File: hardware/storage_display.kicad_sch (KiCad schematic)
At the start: 14 parts, among them J2 microSD, J3 OLED 1.27in 128x96

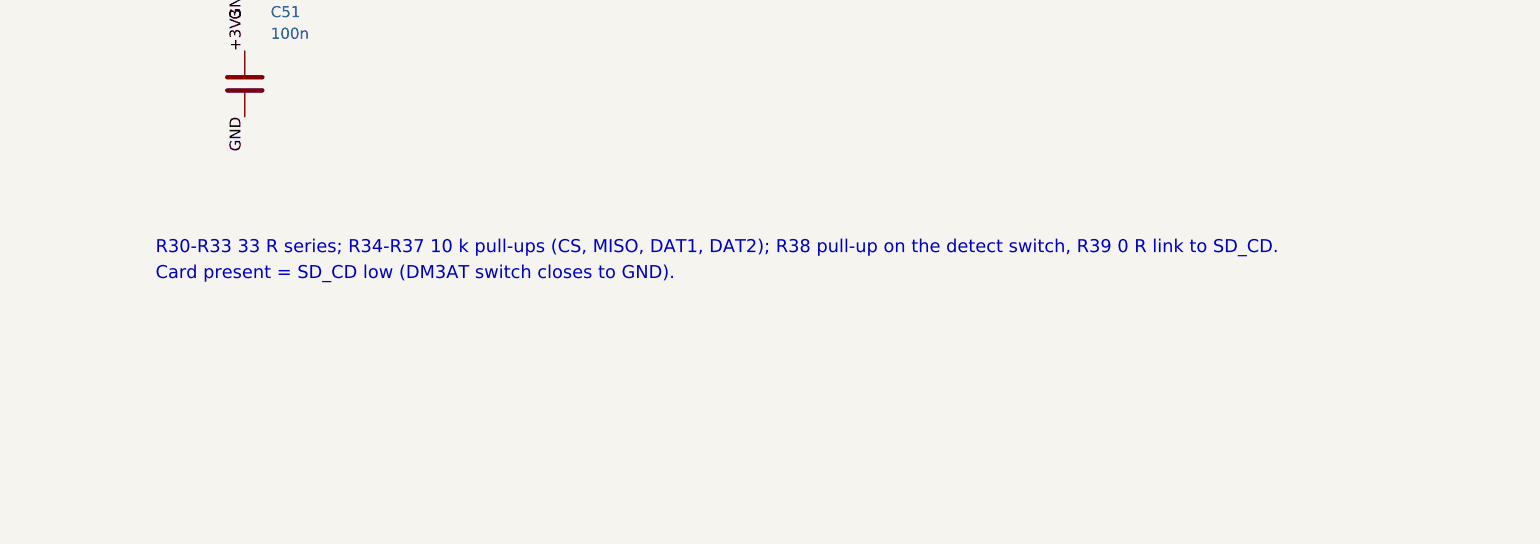
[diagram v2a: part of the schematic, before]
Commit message: BOM cost optimisation against the JLCPCB catalog; schematic-side regulator fix
jlc_price.py prices the BOM via JLCPCB's parts API. Substitutions cut parts+fees
per board from $32.95 to $17.19 on a 10-board run: PSRAM DNP, electrolytic bulk
caps, TF-01A socket, PJ-320D jack, 74HC574, GD25Q128E, 0603 10 uF, basic LED,
preferred MCP6002; U16 decoder deleted (strobes on GPIO), U8 and U15 become
74LVC245s; J3/J5 hand-soldered. Adds the AOTA inductor and VREG_AVDD filter.
PCB needs a relayout; fab/ is stale.

Co-Authored-By: Claude Fable 5.1 <noreply@anthropic.com>
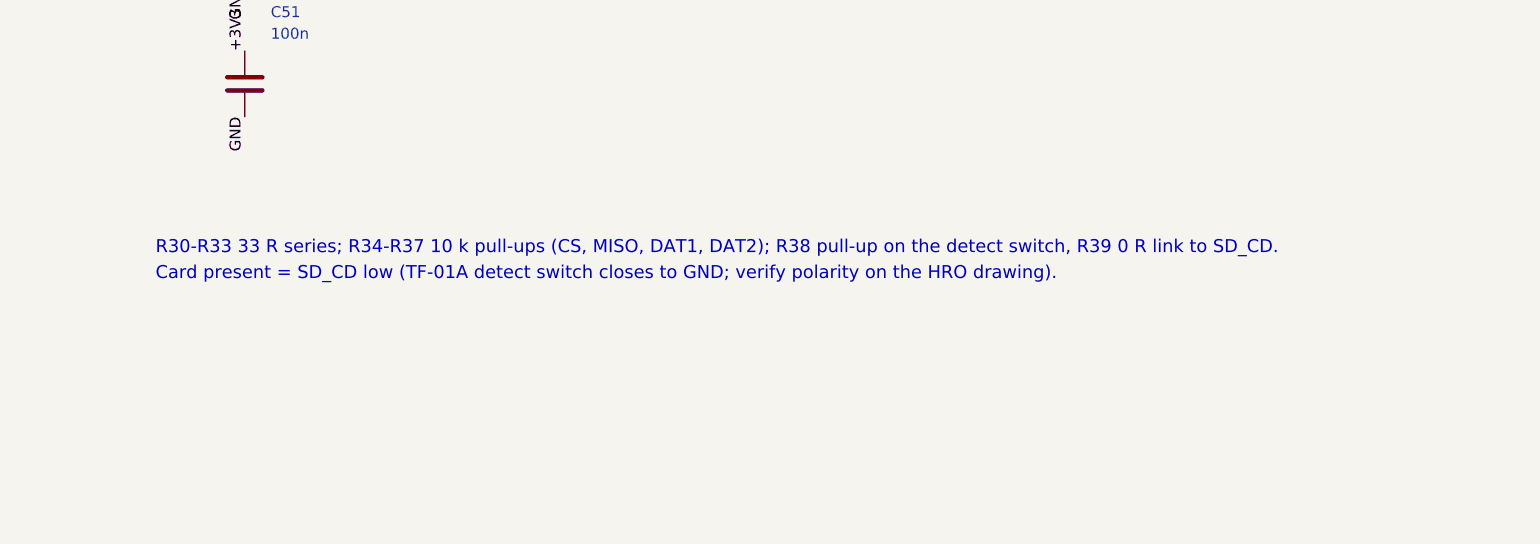
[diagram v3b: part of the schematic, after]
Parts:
- C50: footprint Capacitor_SMD:C_0805_2012Metric -> Capacitor_SMD:C_0603_1608Metric; LCSC C15850 -> C19702; MPN CL21A106KAYNNNE -> CL10A106KP8NNNC
- J2: footprint Connector_Card:microSD_HC_Hirose_DM3AT-SF-PEJM5 -> TSPico:microSD_TF-01A; LCSC C114218 -> C91145; MPN DM3AT-SF-PEJM5 -> TF-01A
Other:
- note added: "Card present = SD_CD low (TF-01A detect switch closes to GND; verify polarity on the HRO drawing)."
- note removed: "Card present = SD_CD low (DM3AT switch closes to GND)."
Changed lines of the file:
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@@
     (property "Reference" "J2" (at 103.33 85.67 0) (effects (font (size 1.27 1.27)) (justify left)))
     (property "Value" "microSD" (at 103.33 88.17 0) (effects (font (size 1.27 1.27)) (justify left)))
-    (property "Footprint" "Connector_Card:microSD_HC_Hirose_DM3AT-SF-PEJM5" (at 100.33 100.33 0) (effects (font (size 1.27 1.27)) (justify left) (hide yes)))
+    (property "Footprint" "TSPico:microSD_TF-01A" (at 100.33 100.33 0) (effects (font (size 1.27 1.27)) (justify left) (hide yes)))
     (property "Datasheet" "" (at 100.33 100.33 0) (effects (font (size 1.27 1.27)) (justify left) (hide yes)))
     (property "Description" "" (at 100.33 100.33 0) (effects (font (size 1.27 1.27)) (justify left) (hide yes)))
-    (property "MPN" "DM3AT-SF-PEJM5" (at 100.33 100.33 0) (effects (font (size 1.27 1.27)) (justify left) (hide yes)))
-    (property "LCSC" "C114218" (at 100.33 100.33 0) (effects (font (size 1.27 1.27)) (justify left) (hide yes)))
+    (property "MPN" "TF-01A" (at 100.33 100.33 0) (effects (font (size 1.27 1.27)) (justify left) (hide yes)))
+    (property "LCSC" "C91145" (at 100.33 100.33 0) (effects (font (size 1.27 1.27)) (justify left) (hide yes)))
     (pin "1")
     (pin "2")
@@
     (property "Reference" "C50" (at 103.33 141.55 0) (effects (font (size 1.27 1.27)) (justify left)))
     (property "Value" "10u" (at 103.33 144.05 0) (effects (font (size 1.27 1.27)) (justify left)))
-    (property "Footprint" "Capacitor_SMD:C_0805_2012Metric" (at 100.33 149.86 0) (effects (font (size 1.27 1.27)) (justify left) (hide yes)))
+    (property "Footprint" "Capacitor_SMD:C_0603_1608Metric" (at 100.33 149.86 0) (effects (font (size 1.27 1.27)) (justify left) (hide yes)))
     (property "Datasheet" "" (at 100.33 149.86 0) (effects (font (size 1.27 1.27)) (justify left) (hide yes)))
     (property "Description" "" (at 100.33 149.86 0) (effects (font (size 1.27 1.27)) (justify left) (hide yes)))
-    (property "MPN" "CL21A106KAYNNNE" (at 100.33 149.86 0) (effects (font (size 1.27 1.27)) (justify left) (hide yes)))
-    (property "LCSC" "C15850" (at 100.33 149.86 0) (effects (font (size 1.27 1.27)) (justify left) (hide yes)))
+    (property "MPN" "CL10A106KP8NNNC" (at 100.33 149.86 0) (effects (font (size 1.27 1.27)) (justify left) (hide yes)))
+    (property "LCSC" "C19702" (at 100.33 149.86 0) (effects (font (size 1.27 1.27)) (justify left) (hide yes)))
     (pin "1")
     (pin "2")
@@
   (label "GND" (at 100.33 168.91 270) (effects (font (size 1.27 1.27)) (justify right bottom)))
   (text "R30-R33 33 R series; R34-R37 10 k pull-ups (CS, MISO, DAT1, DAT2); R38 pull-up on the detect switch, R39 0 R link to SD_CD." (exclude_from_sim no) (at 90 185 0) (effects (font (size 1.5 1.5)) (justify left bottom)))
-  (text "Card present = SD_CD low (DM3AT switch closes to GND)." (exclude_from_sim no) (at 90 188 0) (effects (font (size 1.5 1.5)) (justify left bottom)))
+  (text "Card present = SD_CD low (TF-01A detect switch closes to GND; verify polarity on the HRO drawing)." (exclude_from_sim no) (at 90 188 0) (effects (font (size 1.5 1.5)) (justify left bottom)))
   (symbol (lib_id "Connector_Generic:Conn_01x07") (at 299.72 110.49 0) (unit 1)
     (exclude_from_sim no) (in_bom yes) (on_board yes) (dnp no)

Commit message: Relayout: 130 x 64.25 mm board with the consolidated logic and cheaper BOM
Regulator and crystal hand-routed per the RP2350 design guide (locked
pre-routes), TF-01A socket flush with the edge, custom footprints from LCSC
land patterns, 0.15 mm signal tracks, 0.6/0.3 vias throughout. New flow:
gen_layout -> preroute -> autoroute -> finish. Zero DRC violations; open are
two nets of the unfitted DMA option (nMRD, nWR_ALO). Fab outputs regenerated.

Co-Authored-By: Claude Fable 5.1 <noreply@anthropic.com>
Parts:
- J2: footprint TSPico:microSD_TF-01A -> tspico:microSD_TF-01A
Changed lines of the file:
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@@
     (property "Reference" "J2" (at 103.33 85.67 0) (effects (font (size 1.27 1.27)) (justify left)))
     (property "Value" "microSD" (at 103.33 88.17 0) (effects (font (size 1.27 1.27)) (justify left)))
-    (property "Footprint" "TSPico:microSD_TF-01A" (at 100.33 100.33 0) (effects (font (size 1.27 1.27)) (justify left) (hide yes)))
+    (property "Footprint" "tspico:microSD_TF-01A" (at 100.33 100.33 0) (effects (font (size 1.27 1.27)) (justify left) (hide yes)))
     (property "Datasheet" "" (at 100.33 100.33 0) (effects (font (size 1.27 1.27)) (justify left) (hide yes)))
     (property "Description" "" (at 100.33 100.33 0) (effects (font (size 1.27 1.27)) (justify left) (hide yes)))

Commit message: v3 prototype 2: bus pull-ups, SD socket power switch, PSRAM footprint
Fixes from proto1 bring-up and issue #21:

- R14 2k2 from nBE (edge A29) to +5V_EDGE. The 74LVC06 only pulls /BE
  low; without a pull-up it rose too slowly and a RAM opcode fetch after
  a served byte read wrong bits. Same value as the bodge on board 1.
- R15-R17 10k pull-ups on GP8-GP10 (nAEN_LO, nAEN_HI, nDATA_OE). The
  RP2350 resets its pads with pull-downs, so in reset and BOOTSEL all
  three buffers were enabled and U1 and U2 both drove MD.
- U32 SY6280AAC current-limited switch on the SD socket's VDD (+3V3_SD),
  enabled from XL9555 P0.6 (SD_PWR_EN), held off by R43 until the
  firmware sets it; R42 15k sets 0.45 A. A card that latches up hits the
  limit instead of pulling +3V3 down and resetting the RP2350B, and a
  wedged card can be power-cycled. R34-R37 move to +3V3_SD so they cannot
  power a switched-off card; the detect pull-up R38 stays on +3V3.
  Firmware: power on after the detect switch reads a card and before any
  SPI; release the SD pins before powering off.
- U22 footprint SOIC-8 3.9 x 4.9 mm. The APS6404L-3SQR-SN is SOP-8
  150 mil (AP Memory package code SN); proto1 had the 208 mil footprint.
  Still DNP; ESP-PSRAM64H (Adafruit 4677) fits the same pads by hand.

Routed by flow.py on the first attempt, DRC clean at every severity
(2119 segments, 385 vias). ERC: the one pre-existing U4 warning only.
$14.90/board at 10 with fees. PSRAM options surveyed in
docs/bom-cost-optimization.md.

Co-Authored-By: Claude Opus 5.5 <noreply@anthropic.com>
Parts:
- added C52: 1u, Capacitor_SMD:C_0603_1608Metric, symbol Device:C
- added R42: 15k, Resistor_SMD:R_0603_1608Metric, symbol Device:R
- added R43: 10k, Resistor_SMD:R_0603_1608Metric, symbol Device:R
- added U32: SY6280AAC, Package_TO_SOT_SMD:SOT-23-5, symbol Power_Management:AAT4610BIGV-1-T1
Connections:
- net +3V3: now also C52.1, U32.5 (IN); no longer C50.1, C51.1, J2.4 (VDD), R34.1, R35.1, R36.1, R37.1
- net GND: now also C52.2, R42.2, R43.2, U32.2 (GND)
- new net +3V3_SD: C50.1, C51.1, J2.4 (VDD), R34.1, R35.1, R36.1, R37.1, U32.1 (OUT)
- new net SD_ISET: R42.1, U32.3 (SET)
- new net SD_PWR_EN: R43.1, U32.4 (ON)
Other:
- note added: "Card present = SD_CD low (the TF-01A switch closes to GND; confirmed on proto1). U32: SD VDD switch, R42 sets 0.45 A, R43 holds it off."
- note added: "Firmware order: card detected, settle, SD_PWR_EN on, then SPI. SPI lines released (inputs) before SD_PWR_EN goes off."
- note added: "R30-R33 33 R series; R34-R37 10 k pull-ups (CS, MISO, DAT1, DAT2) on +3V3_SD; R38 pull-up on the detect switch (+3V3), R39 0 R link to SD_CD."
- note removed: "Card present = SD_CD low (TF-01A detect switch closes to GND; verify polarity on the HRO drawing)."
- note removed: "R30-R33 33 R series; R34-R37 10 k pull-ups (CS, MISO, DAT1, DAT2); R38 pull-up on the detect switch, R39 0 R link to SD_CD."

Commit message: v3 proto3: male DE-9, I2C OLED header, buttons in a 2x2 block
- J5: male DE-9 (CONNFLY DS1037-09MNAKT74-0CC, C75750). Atari sticks end
  in a female plug; proto1/2's female footprint mirrors every pin under a
  male part, putting the stick's ground on pin 7 (JOY_5V, open), so nothing
  read. Same body position and mounting holes as proto2.
- J3: 1x4 header for a 1.54in 128x64 SSD1309 I2C module (1 GND, 2 +3V3,
  3 SCL GP43, 4 SDA GP42) on I2C1, R44/R45 4k7 pull-ups. Replaces the 7-pin
  SSD1351 SPI header; GP34, GP41 and expander P0.2 (with R11) are freed.
- SW3 under SW1, SW4 under SW2, so the module covers no buttons; D4/R5
  move left of the ESP32, between H1 and the USB-C socket.

Routed by flow.py on the first attempt: DRC clean at every severity,
2125 segments, 373 vias. ERC: the one existing U4 warning.

Co-Authored-By: Claude Opus 5.5 <noreply@anthropic.com>
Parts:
- removed J3: OLED 1.27in 128x96, Connector_PinHeader_2.54mm:PinHeader_1x07_P2.54mm_Vertical, symbol Connector_Generic:Conn_01x07
- added J3: OLED 1.54in 128x64 I2C, Connector_PinHeader_2.54mm:PinHeader_1x04_P2.54mm_Vertical, symbol Connector_Generic:Conn_01x04
- added R44, R45: 4k7, Resistor_SMD:R_0603_1608Metric, symbol Device:R
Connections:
- net +3V3: now also J3.2 (Pin_2), R44.1, R45.1
- net GND: now also J3.1 (Pin_1)
- new net OLED_SCL: J3.3 (Pin_3), R44.2
- new net OLED_SDA: J3.4 (Pin_4), R45.2
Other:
- note added: "J3 pin order matches the module: GND VCC SCL SDA. VCC is +3V3, so the module's own pull-ups stay at 3.3 V."
- note added: "OLED: 4-pin header for a 1.54in 128x64 SSD1309 I2C module on I2C1 (GP42 SDA, GP43 SCL), its own bus so display updates never delay joystick reads."
- note removed: "J3 pin order matches the Waveshare module: VCC GND DIN CLK CS DC RST."
- note removed: "OLED: 7-pin header for the Waveshare 1.27in 128x96 SSD1351 module on SPI1 (GP40-GP43), reset from CTL."
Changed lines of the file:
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@@
   (title_block (title "TS-Pico v3: SD and Display") (rev "0.1") (company "Timex/Sinclair Online User Group"))
   (text "Micro SD in SPI mode on the RP2350B SPI0 (GP36-GP39); card detect (switch to GND) into STAT bit 7." (exclude_from_sim no) (at 20 285 0) (effects (font (size 2.5 2.5)) (justify left bottom)))
-  (text "OLED: 7-pin header for the Waveshare 1.27in 128x96 SSD1351 module on SPI1 (GP40-GP43), reset from CTL." (exclude_from_sim no) (at 20 290 0) (effects (font (size 2.0 2.0)) (justify left bottom)))
+  (text "OLED: 4-pin header for a 1.54in 128x64 SSD1309 I2C module on I2C1 (GP42 SDA, GP43 SCL), its own bus so display updates never delay joystick reads." (exclude_from_sim no) (at 20 290 0) (effects (font (size 2.0 2.0)) (justify left bottom)))
   (symbol (lib_id "power:+3V3") (at 299.72 30.48 0) (unit 1)
     (exclude_from_sim no) (in_bom yes) (on_board yes) (dnp no)
@@
   (text "Card present = SD_CD low (the TF-01A switch closes to GND; confirmed on proto1). U32: SD VDD switch, R42 sets 0.45 A, R43 holds it off." (exclude_from_sim no) (at 90 188 0) (effects (font (size 1.5 1.5)) (justify left bottom)))
   (text "Firmware order: card detected, settle, SD_PWR_EN on, then SPI. SPI lines released (inputs) before SD_PWR_EN goes off." (exclude_from_sim no) (at 90 191 0) (effects (font (size 1.5 1.5)) (justify left bottom)))
-  (symbol (lib_id "Connector_Generic:Conn_01x07") (at 299.72 110.49 0) (unit 1)
-    (exclude_from_sim no) (in_bom yes) (on_board yes) (dnp no)
-    (property "Reference" "J3" (at 302.72 98.37 0) (effects (font (size 1.27 1.27)) (justify left)))
-    (property "Value" "OLED 1.27in 128x96" (at 302.72 100.87 0) (effects (font (size 1.27 1.27)) (justify left)))
-    (property "Footprint" "Connector_PinHeader_2.54mm:PinHeader_1x07_P2.54mm_Vertical" (at 299.72 110.49 0) (effects (font (size 1.27 1.27)) (justify left) (hide yes)))
+  (symbol (lib_id "Connector_Generic:Conn_01x04") (at 299.72 110.49 0) (unit 1)
+    (exclude_from_sim no) (in_bom yes) (on_board yes) (dnp no)
+    (property "Reference" "J3" (at 302.72 103.45 0) (effects (font (size 1.27 1.27)) (justify left)))
+    (property "Value" "OLED 1.54in 128x64 I2C" (at 302.72 105.95 0) (effects (font (size 1.27 1.27)) (justify left)))
+    (property "Footprint" "Connector_PinHeader_2.54mm:PinHeader_1x04_P2.54mm_Vertical" (at 299.72 110.49 0) (effects (font (size 1.27 1.27)) (justify left) (hide yes)))
     (property "Datasheet" "" (at 299.72 110.49 0) (effects (font (size 1.27 1.27)) (justify left) (hide yes)))
     (property "Description" "" (at 299.72 110.49 0) (effects (font (size 1.27 1.27)) (justify left) (hide yes)))
-    (property "MPN" "2.54-1x40P (cut to 7)" (at 299.72 110.49 0) (effects (font (size 1.27 1.27)) (justify left) (hide yes)))
+    (property "MPN" "2.54-1x40P (cut to 4)" (at 299.72 110.49 0) (effects (font (size 1.27 1.27)) (justify left) (hide yes)))
     (property "LCSC" "C2337" (at 299.72 110.49 0) (effects (font (size 1.27 1.27)) (justify left) (hide yes)))
     (pin "1")
@@
     (pin "3")
     (pin "4")
-    (pin "5")
-    (pin "6")
-    (pin "7")
     (instances (project "tspico-v3" (path "/9088d141-8624-4d5c-91a9-7a3a7a90b3cc/93fed0fb-db78-4462-a3db-90a4c9868f58" (reference "J3") (unit 1))))
   )
-  (label "+3V3" (at 294.64 102.87 180) (effects (font (size 1.27 1.27)) (justify right bottom)))
-  (label "GND" (at 294.64 105.41 180) (effects (font (size 1.27 1.27)) (justify right bottom)))
-  (global_label "OLED_MOSI" (shape input) (at 294.64 107.95 180) (effects (font (size 1.27 1.27)) (justify right)))
-  (global_label "OLED_SCK" (shape input) (at 294.64 110.49 180) (effects (font (size 1.27 1.27)) (justify right)))
-  (global_label "OLED_CS" (shape input) (at 294.64 113.03 180) (effects (font (size 1.27 1.27)) (justify right)))
-  (global_label "OLED_DC" (shape input) (at 294.64 115.57 180) (effects (font (size 1.27 1.27)) (justify right)))
-  (global_label "nOLED_RST" (shape input) (at 294.64 118.11 180) (effects (font (size 1.27 1.27)) (justify right)))
-  (text "J3 pin order matches the Waveshare module: VCC GND DIN CLK CS DC RST." (exclude_from_sim no) (at 280 135 0) (effects (font (size 1.5 1.5)) (justify left bottom)))
+  (label "GND" (at 294.64 107.95 180) (effects (font (size 1.27 1.27)) (justify right bottom)))
+  (label "+3V3" (at 294.64 110.49 180) (effects (font (size 1.27 1.27)) (justify right bottom)))
+  (global_label "OLED_SCL" (shape input) (at 294.64 113.03 180) (effects (font (size 1.27 1.27)) (justify right)))
+  (global_label "OLED_SDA" (shape bidirectional) (at 294.64 115.57 180) (effects (font (size 1.27 1.27)) (justify right)))
+  (symbol (lib_id "Device:R") (at 330.2 149.86 0) (unit 1)
+    (exclude_from_sim no) (in_bom yes) (on_board yes) (dnp no)
+    (property "Reference" "R44" (at 333.2 141.55 0) (effects (font (size 1.27 1.27)) (justify left)))
+    (property "Value" "4k7" (at 333.2 144.05 0) (effects (font (size 1.27 1.27)) (justify left)))
+    (property "Footprint" "Resistor_SMD:R_0603_1608Metric" (at 330.2 149.86 0) (effects (font (size 1.27 1.27)) (justify left) (hide yes)))
+    (property "Datasheet" "" (at 330.2 149.86 0) (effects (font (size 1.27 1.27)) (justify left) (hide yes)))
+    (property "Description" "" (at 330.2 149.86 0) (effects (font (size 1.27 1.27)) (justify left) (hide yes)))
+    (property "MPN" "0603WAF4701T5E" (at 330.2 149.86 0) (effects (font (size 1.27 1.27)) (justify left) (hide yes)))
+    (property "LCSC" "C23162" (at 330.2 149.86 0) (effects (font (size 1.27 1.27)) (justify left) (hide yes)))
+    (pin "1")
+    (pin "2")
+    (instances (project "tspico-v3" (path "/9088d141-8624-4d5c-91a9-7a3a7a90b3cc/93fed0fb-db78-4462-a3db-90a4c9868f58" (reference "R44") (unit 1))))
+  )
+  (label "+3V3" (at 330.20 146.05 90) (effects (font (size 1.27 1.27)) (justify left bottom)))
+  (global_label "OLED_SCL" (shape bidirectional) (at 330.20 153.67 270) (effects (font (size 1.27 1.27)) (justify right)))
+  (symbol (lib_id "Device:R") (at 345.44 149.86 0) (unit 1)
+    (exclude_from_sim no) (in_bom yes) (on_board yes) (dnp no)
+    (property "Reference" "R45" (at 348.44 141.55 0) (effects (font (size 1.27 1.27)) (justify left)))
+    (property "Value" "4k7" (at 348.44 144.05 0) (effects (font (size 1.27 1.27)) (justify left)))
+    (property "Footprint" "Resistor_SMD:R_0603_1608Metric" (at 345.44 149.86 0) (effects (font (size 1.27 1.27)) (justify left) (hide yes)))
+    (property "Datasheet" "" (at 345.44 149.86 0) (effects (font (size 1.27 1.27)) (justify left) (hide yes)))
+    (property "Description" "" (at 345.44 149.86 0) (effects (font (size 1.27 1.27)) (justify left) (hide yes)))
+    (property "MPN" "0603WAF4701T5E" (at 345.44 149.86 0) (effects (font (size 1.27 1.27)) (justify left) (hide yes)))
+    (property "LCSC" "C23162" (at 345.44 149.86 0) (effects (font (size 1.27 1.27)) (justify left) (hide yes)))
+    (pin "1")
+    (pin "2")
+    (instances (project "tspico-v3" (path "/9088d141-8624-4d5c-91a9-7a3a7a90b3cc/93fed0fb-db78-4462-a3db-90a4c9868f58" (reference "R45") (unit 1))))
+  )
+  (label "+3V3" (at 345.44 146.05 90) (effects (font (size 1.27 1.27)) (justify left bottom)))
+  (global_label "OLED_SDA" (shape bidirectional) (at 345.44 153.67 270) (effects (font (size 1.27 1.27)) (justify right)))
+  (text "J3 pin order matches the module: GND VCC SCL SDA. VCC is +3V3, so the module's own pull-ups stay at 3.3 V." (exclude_from_sim no) (at 280 135 0) (effects (font (size 1.5 1.5)) (justify left bottom)))
   (embedded_fonts no)
 )
